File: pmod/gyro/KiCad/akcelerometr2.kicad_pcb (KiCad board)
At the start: 2 copper layers, 24.4 x 22.4 mm, 5 parts, among them J2 Conn_01x04_Pin, J3 Conn_01x04_Pin, J4 Conn_01x08_Pin

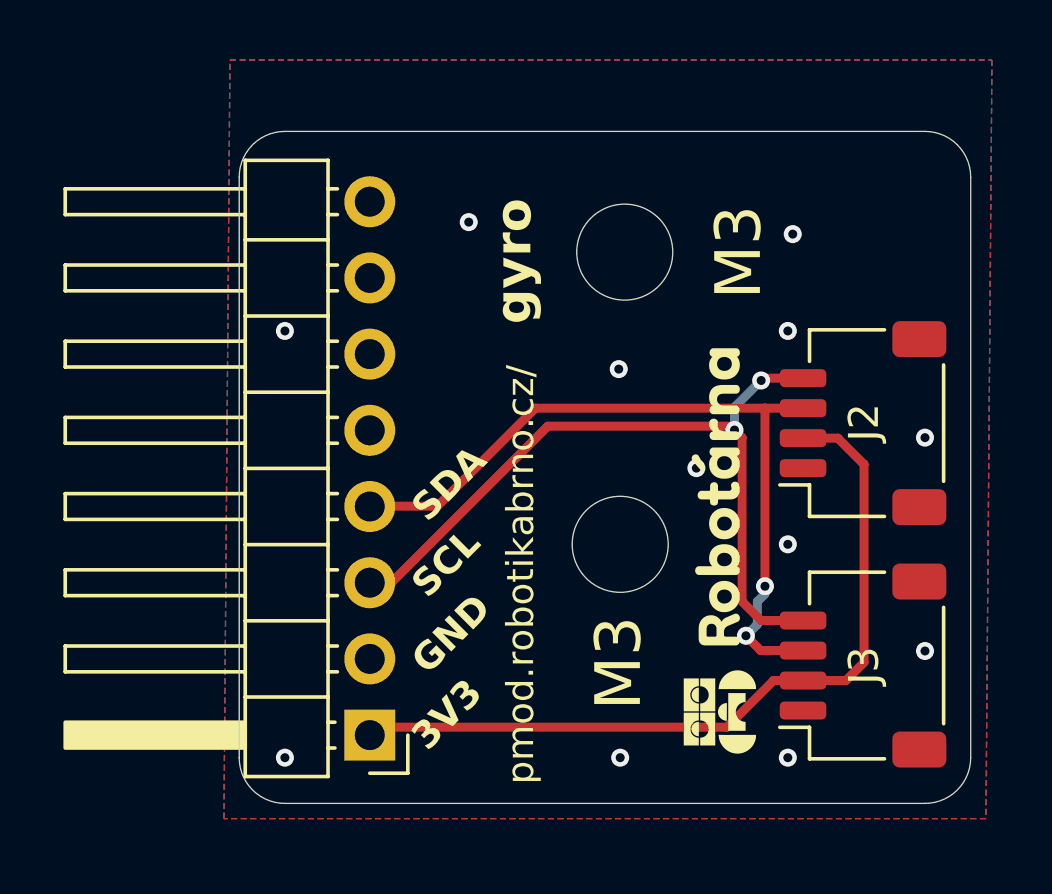
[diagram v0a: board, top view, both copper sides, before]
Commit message: fix: Pridal jsem opravy, ktere byly navrzene
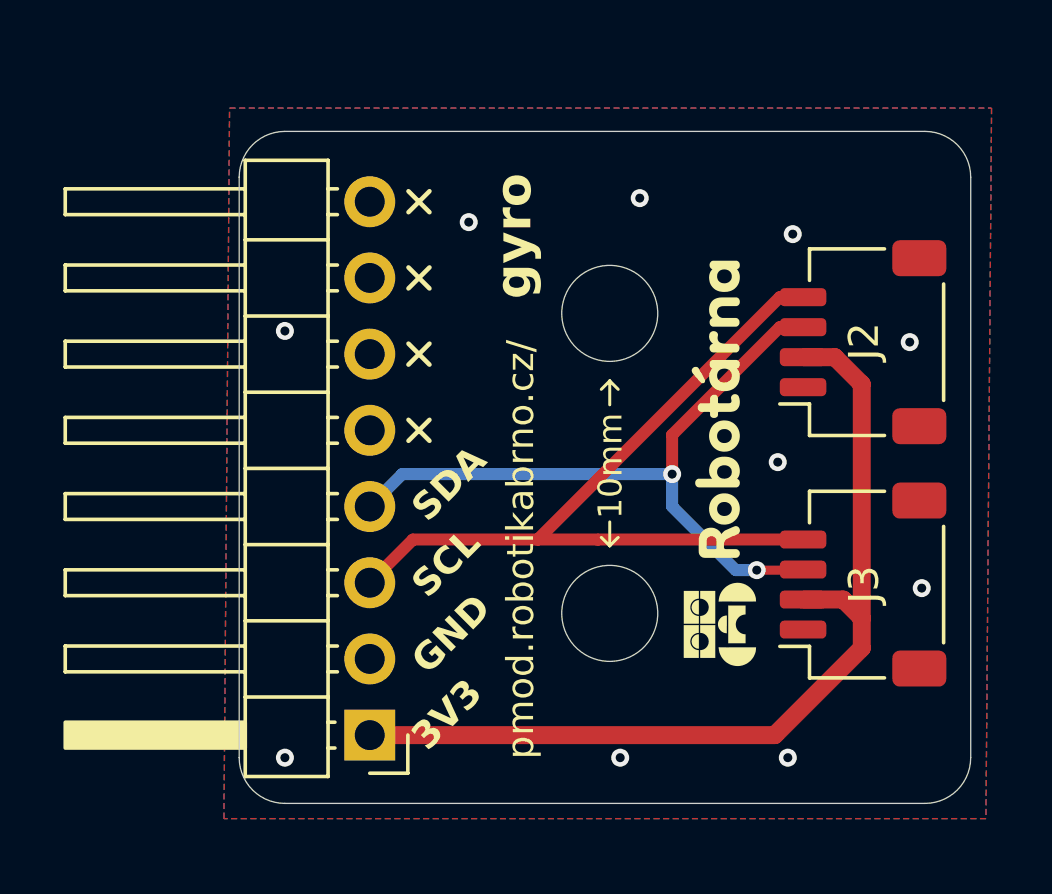
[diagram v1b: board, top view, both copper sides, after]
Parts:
- moved J2 2.70 mm to (125.4, 72.0)
- moved J3 2.70 mm to (125.4, 80.1)
- moved H2 2.33 mm to (117.0, 81.0)
- moved H1 2.10 mm to (117.0, 71.0)
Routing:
- net +3V3: track 26.5 -> 31.0 mm
- net SDA: track 25.7 -> 24.0 mm
- net SCL: track 26.0 -> 27.3 mm, vias 2 -> 0
- net GND: vias 12 -> 10
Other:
- board text added: "10mm"
- board text removed: "M3"

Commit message: fix: prepare all board for manufacturing
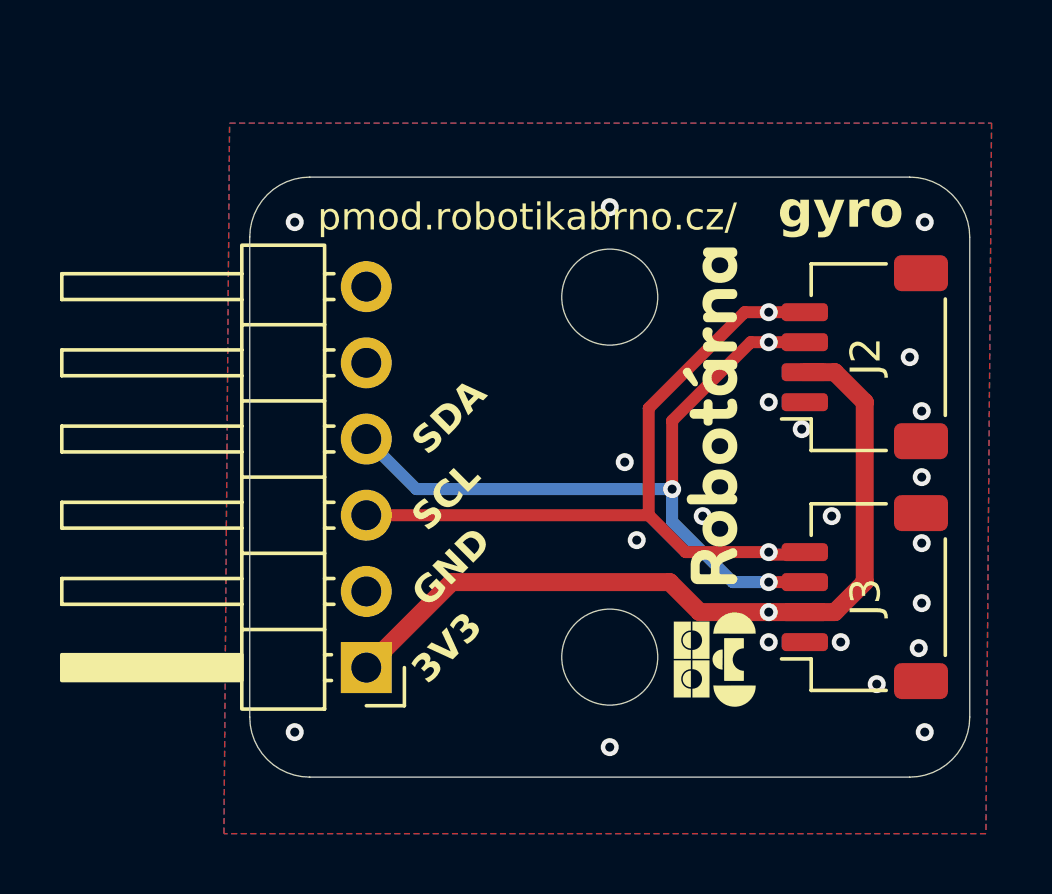
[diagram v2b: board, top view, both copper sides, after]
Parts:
- J4: footprint Connector_PinHeader_2.54mm:PinHeader_1x08_P2.54mm_Horizontal -> Connector_PinHeader_2.54mm:PinHeader_1x06_P2.54mm_Horizontal
- moved J4 2.25 mm to (108.9, 82.8)
- moved H2 1.46 mm to (117.0, 82.5)
- moved H1 0.54 mm to (117.0, 70.5)
- moved J2 0.50 mm to (125.5, 72.5)
- moved J3 0.42 mm to (125.5, 80.5)
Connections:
- J2 pad MP: (no net) -> GND
- J3 pad MP: (no net) -> GND
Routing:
- net +3V3: track 31.0 -> 27.1 mm, vias 0 -> 1
- net SCL: track 27.3 -> 25.1 mm, vias 0 -> 2
- net SDA: track 24.0 -> 24.9 mm, vias 2 -> 3
- net GND: track 0.00 -> 0.04 mm, vias 10 -> 21
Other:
- board size 24.4 x 22.4 mm -> 24 x 20 mm
- board text added: "20mm"
- board text added: "24mm"
- board text removed: "10mm"
- board text removed: "H2"

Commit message: docs: add images, fix docs
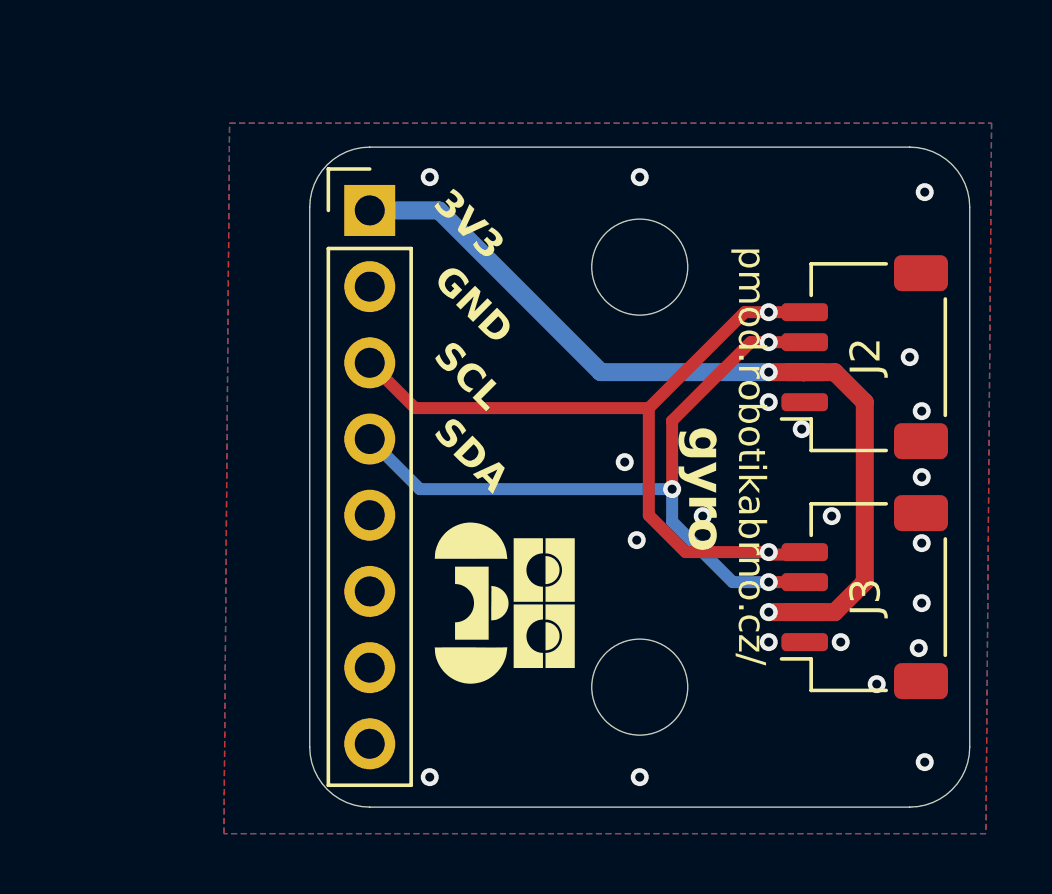
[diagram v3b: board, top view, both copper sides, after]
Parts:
- J4: value Conn_01x08_Pin -> Conn_01x06_Pin; footprint Connector_PinHeader_2.54mm:PinHeader_1x06_P2.54mm_Horizontal -> Connector_PinHeader_2.54mm:PinHeader_1x08_P2.54mm_Vertical
- moved J4 15.2 mm to (109.0, 67.6), turned to 0 degrees
- moved H1 1.41 mm to (118.0, 69.5)
- moved H2 1.41 mm to (118.0, 83.5)
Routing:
- net +3V3: track 27.1 -> 28.8 mm, vias 1 -> 2
- net SCL: track 25.1 -> 25.7 mm
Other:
- board size 24 x 20 mm -> 22 x 22 mm
